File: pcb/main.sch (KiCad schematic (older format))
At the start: 57 parts, among them J1 Barrel_Jack, J2 NXC digit iface, J3 NXC num iface, J4 Conn_01x03, J5 ICSP, SW1 Tactile SPST, SW2 Tactile SPST, SW3 Tactile SPST, U1 CD4028, U2 NCP1117, U3 PIC24FV32KA302-I_SO, U4 DS1307Z+, Y1 8 MHz, Y2 32.768 kHz

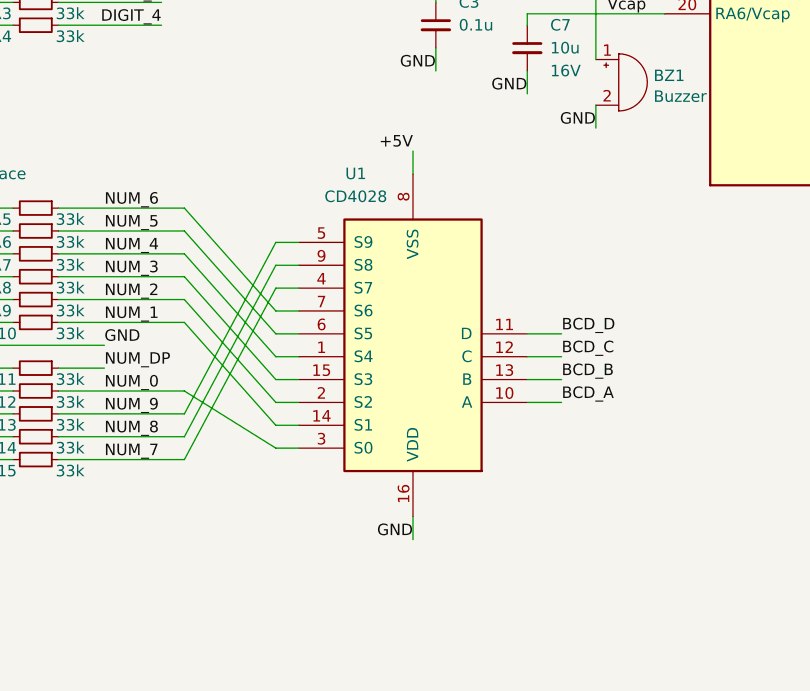
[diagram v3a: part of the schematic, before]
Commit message: Fix some problems with pcb, crystals and rectifier using wrong footprints. Octal decoder had Vss and Vdd swapped.
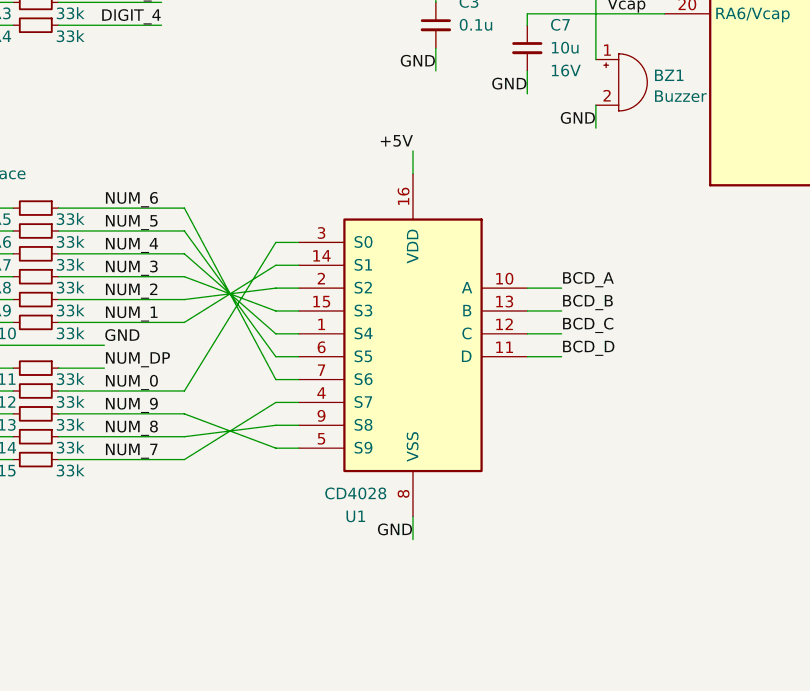
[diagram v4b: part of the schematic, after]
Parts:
- D1: footprint Diodes_SMD:Diode_Bridge_MBLS -> nixie-clock:Diode-SMC_KMB22S-MBS
- Y1: footprint Crystals:Crystal_SMD_5032-2pin_5.0x3.2mm_HandSoldering -> nixie-clock:Crystal-Abracom_ABM3-5.0x3.2
- Y2: footprint Crystals:Crystal_SMD_5032-2pin_5.0x3.2mm_HandSoldering -> nixie-clock:Crystal-Vectron_VMK3-3.2x1.5
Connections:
- net +5V: now also U1.16 (VDD); no longer U1.8 (VSS)
- net GND: now also U1.8 (VSS); no longer U1.16 (VDD)
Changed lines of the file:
@@
 F 0 "D1" V 2850 1850 50  0000 R CNN
 F 1 "KMB22S" V 2750 1850 50  0000 R CNN
-F 2 "Diodes_SMD:Diode_Bridge_MBLS" H 2500 1450 50  0001 C CNN
+F 2 "nixie-clock:Diode-SMC_KMB22S-MBS" H 2500 1450 50  0001 C CNN
 F 3 "http://www.smc-diodes.com/propdf/KMB22S%20THRU%20KMB225S%20N1952%20REV.A.pdf" H 2500 1450 50  0001 C CNN
 F 4 "https://www.digikey.com/en/products/detail/smc-diode-solutions/KMB26STR/7898343" H 2500 1450 50  0001 C CNN "Digikey Page"
@@
 Text Label 7500 4200 0    50   ~ 0
 +5V
-Wire Wire Line
-	4000 5550 3850 5550
-Wire Wire Line
-	4000 5650 3850 5650
-Wire Wire Line
-	4000 5750 3850 5750
-Text Label 4000 5850 0    50   ~ 0
+Text Label 4000 5350 0    50   ~ 0
 BCD_A
-Wire Wire Line
-	4000 5850 3850 5850
 Text Label 3350 4750 2    50   ~ 0
 +5V
-Wire Wire Line
-	3350 4850 3350 4750
 Text Label 3350 6450 2    50   ~ 0
 GND
 Wire Wire Line
-	3350 6350 3350 6450
-Wire Wire Line
-	2750 6050 2350 5800
-Wire Wire Line
-	2750 5850 2350 5400
-Wire Wire Line
-	2750 5650 2350 5200
-Wire Wire Line
-	2750 5550 2350 5100
-Wire Wire Line
-	2750 5450 2350 5000
-Wire Wire Line
-	2750 5350 2350 6100
-Wire Wire Line
-	2750 5150 2350 5900
-Wire Wire Line
-	2750 5250 2350 6000
-Wire Wire Line
-	2750 5950 2350 5500
-Wire Wire Line
-	2750 5750 2350 5300
-Text Label 4000 5750 0    50   ~ 0
+	2750 5150 2350 5800
+Wire Wire Line
+	2750 5350 2350 5400
+Wire Wire Line
+	2750 5550 2350 5200
+Wire Wire Line
+	2750 5650 2350 5100
+Wire Wire Line
+	2750 5750 2350 5000
+Wire Wire Line
+	2750 5850 2350 6100
+Wire Wire Line
+	2750 6050 2350 5900
+Wire Wire Line
+	2750 5950 2350 6000
+Wire Wire Line
+	2750 5250 2350 5500
+Wire Wire Line
+	2750 5450 2350 5300
+Text Label 4000 5450 0    50   ~ 0
 BCD_B
 Text Label 4000 5650 0    50   ~ 0
-BCD_C
-Text Label 4000 5550 0    50   ~ 0
 BCD_D
 Wire Wire Line
@@
 F 0 "Y2" V 7796 3612 50  0000 R CNN
 F 1 "32.768 kHz" V 7705 3612 50  0000 R CNN
-F 2 "Crystals:Crystal_SMD_5032-2pin_5.0x3.2mm_HandSoldering" H 7750 3700 50  0001 C CNN
+F 2 "nixie-clock:Crystal-Vectron_VMK3-3.2x1.5" H 7750 3700 50  0001 C CNN
 F 3 "https://media.digikey.com/pdf/Data%20Sheets/Microchip%20PDFs/VMK3-9005-32K7680000_May15_2021.pdf" H 7750 3700 50  0001 C CNN
 F 4 "https://www.digikey.com/en/products/detail/microchip-technology/VMK3-9005-32K7680000/13175117?s=N4IgjCBcpgbFoDGUBmBDANgZwKYBoQB7KAbXFgA5ZYBOEAXQIAcAXKEAZRYCcBLAOwDmIAL4EALPGghkkdNnxFS4AAw0ATAGYGzNpE48BwsSFoIZqTLgLFIZcWs01tjEK3Zc%2BQ0QTA0KdNKy8tZKdiAqOm56Bl7GBOpgAKyRQZYKNsqa6gB0AOyUAAQA1gASAF5R7voAqvy8LADyKACyOGhYAK7cOD4gALTq5rI8nYq2ZEkMJv0QaXJW48rJkfQi60A" H 7750 3700 50  0001 C CNN "Digikey Page"
@@
 PGED
 NoConn ~ 4450 3650
-$Comp
-L 4xxx:4028 U1
-U 1 1 625F68A2
-P 3350 5650
-F 0 "U1" H 3600 4850 50  0000 C CNN
-F 1 "CD4028" H 3600 4950 50  0000 C CNN
-F 2 "Housings_SOIC:SOIC-16_3.9x9.9mm_Pitch1.27mm" H 3350 5650 50  0001 C CNN
-F 3 "http://www.intersil.com/content/dam/Intersil/documents/cd40/cd4028bms.pdf" H 3350 5650 50  0001 C CNN
-F 4 "https://www.digikey.com/en/products/detail/texas-instruments/CD4028BM96/614903" H 3350 5650 50  0001 C CNN "Digikey Page"
-F 5 "18V" H 3350 5650 50  0001 C CNN "Rating"
-F 6 "-" H 3350 5650 50  0001 C CNN "Alt Datasheet"
-F 7 "-" H 3350 5650 50  0001 C CNN "Alt Digikey"
-	1    3350 5650
-	-1   0    0    1
-$EndComp
-Wire Wire Line
-	2750 6050 2850 6050
-Wire Wire Line
-	2750 5950 2850 5950
-Wire Wire Line
-	2750 5850 2850 5850
-Wire Wire Line
-	2750 5750 2850 5750
-Wire Wire Line
-	2750 5650 2850 5650
-Wire Wire Line
-	2750 5550 2850 5550
-Wire Wire Line
-	2750 5450 2850 5450
-Wire Wire Line
-	2750 5350 2850 5350
-Wire Wire Line
-	2750 5250 2850 5250
-Wire Wire Line
-	2750 5150 2850 5150
 $Sheet
 S 800  2000 1650 950
@@
 F 0 "Y1" H 3950 3950 50  0000 C CNN
 F 1 "8 MHz" H 3950 3850 50  0000 C CNN
-F 2 "Crystals:Crystal_SMD_5032-2pin_5.0x3.2mm_HandSoldering" H 3950 3750 50  0001 C CNN
+F 2 "nixie-clock:Crystal-Abracom_ABM3-5.0x3.2" H 3950 3750 50  0001 C CNN
 F 3 "https://abracon.com/Resonators/abm3.pdf" H 3950 3750 50  0001 C CNN
 F 4 "https://www.digikey.com/en/products/detail/abracon-llc/ABM3-8-000MHZ-D2Y-T/2344570" H 3950 3750 50  0001 C CNN "Digikey Page"
@@
 Wire Wire Line
 	4150 3950 4150 4350
+Wire Wire Line
+	2750 5250 2850 5250
+Wire Wire Line
+	3350 4850 3350 4750
+Wire Wire Line
+	2750 5450 2850 5450
+Wire Wire Line
+	2750 5550 2850 5550
+Wire Wire Line
+	2750 5150 2850 5150
+Wire Wire Line
+	2750 5350 2850 5350
+Wire Wire Line
+	2750 6050 2850 6050
+Wire Wire Line
+	2750 5850 2850 5850
+Wire Wire Line
+	3350 6350 3350 6450
+Wire Wire Line
+	2750 5750 2850 5750
+Wire Wire Line
+	2750 5950 2850 5950
+Wire Wire Line
+	4000 5450 3850 5450
+Wire Wire Line
+	4000 5650 3850 5650
+Wire Wire Line
+	4000 5350 3850 5350
+Wire Wire Line
+	2750 5650 2850 5650
+$Comp
+L 4xxx:4028 U1
+U 1 1 625F68A2
+P 3350 5550
+F 0 "U1" H 3600 4750 50  0000 C CNN
+F 1 "CD4028" H 3600 4850 50  0000 C CNN
+F 2 "Housings_SOIC:SOIC-16_3.9x9.9mm_Pitch1.27mm" H 3350 5550 50  0001 C CNN
+F 3 "http://www.intersil.com/content/dam/Intersil/documents/cd40/cd4028bms.pdf" H 3350 5550 50  0001 C CNN
+F 4 "https://www.digikey.com/en/products/detail/texas-instruments/CD4028BM96/614903" H 3350 5550 50  0001 C CNN "Digikey Page"
+F 5 "18V" H 3350 5550 50  0001 C CNN "Rating"
+F 6 "-" H 3350 5550 50  0001 C CNN "Alt Datasheet"
+F 7 "-" H 3350 5550 50  0001 C CNN "Alt Digikey"
+	1    3350 5550
+	-1   0    0    -1
+$EndComp
+Wire Wire Line
+	4000 5550 3850 5550
+Text Label 4000 5550 0    50   ~ 0
+BCD_C
 $EndSCHEMATC
